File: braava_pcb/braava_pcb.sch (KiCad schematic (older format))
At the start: 49 parts, among them J1 Conn_01x18, J2 Conn_01x18

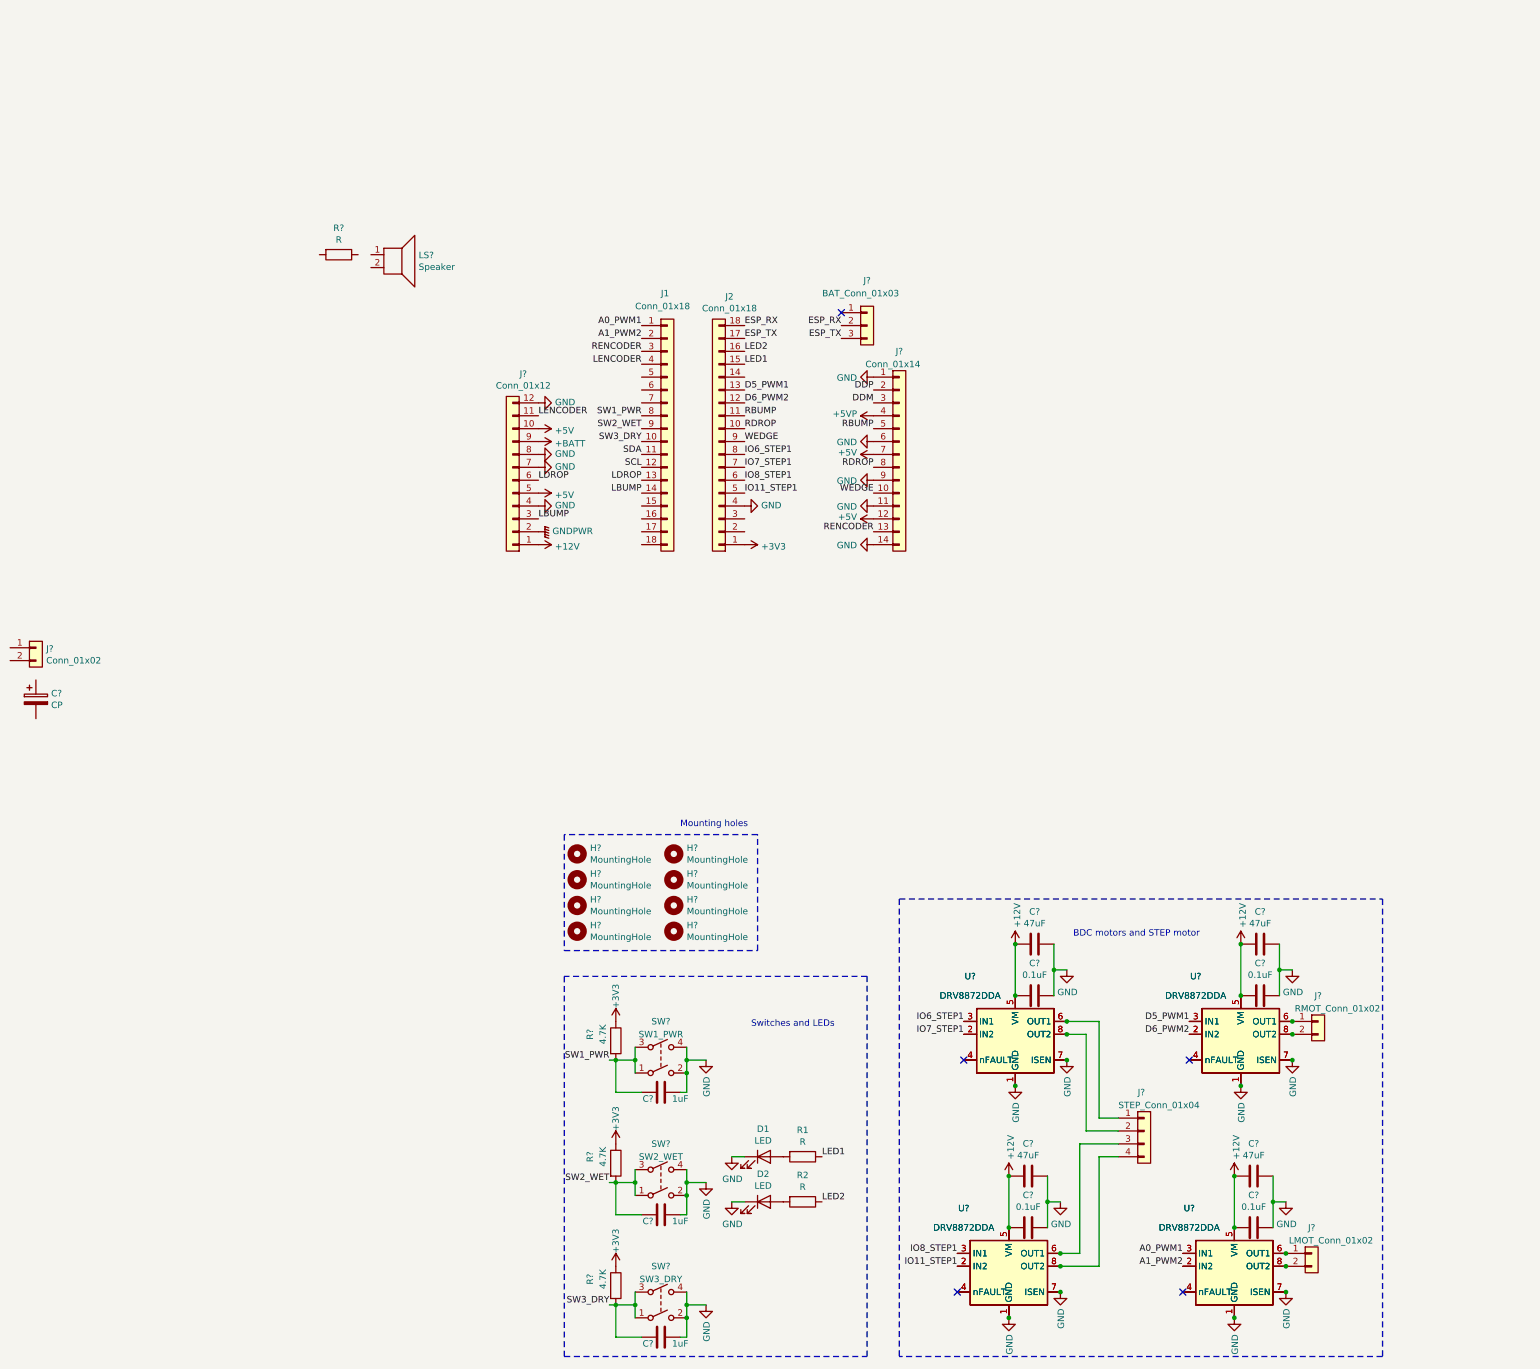
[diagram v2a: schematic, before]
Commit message: Added touch switches library. Started component placement.
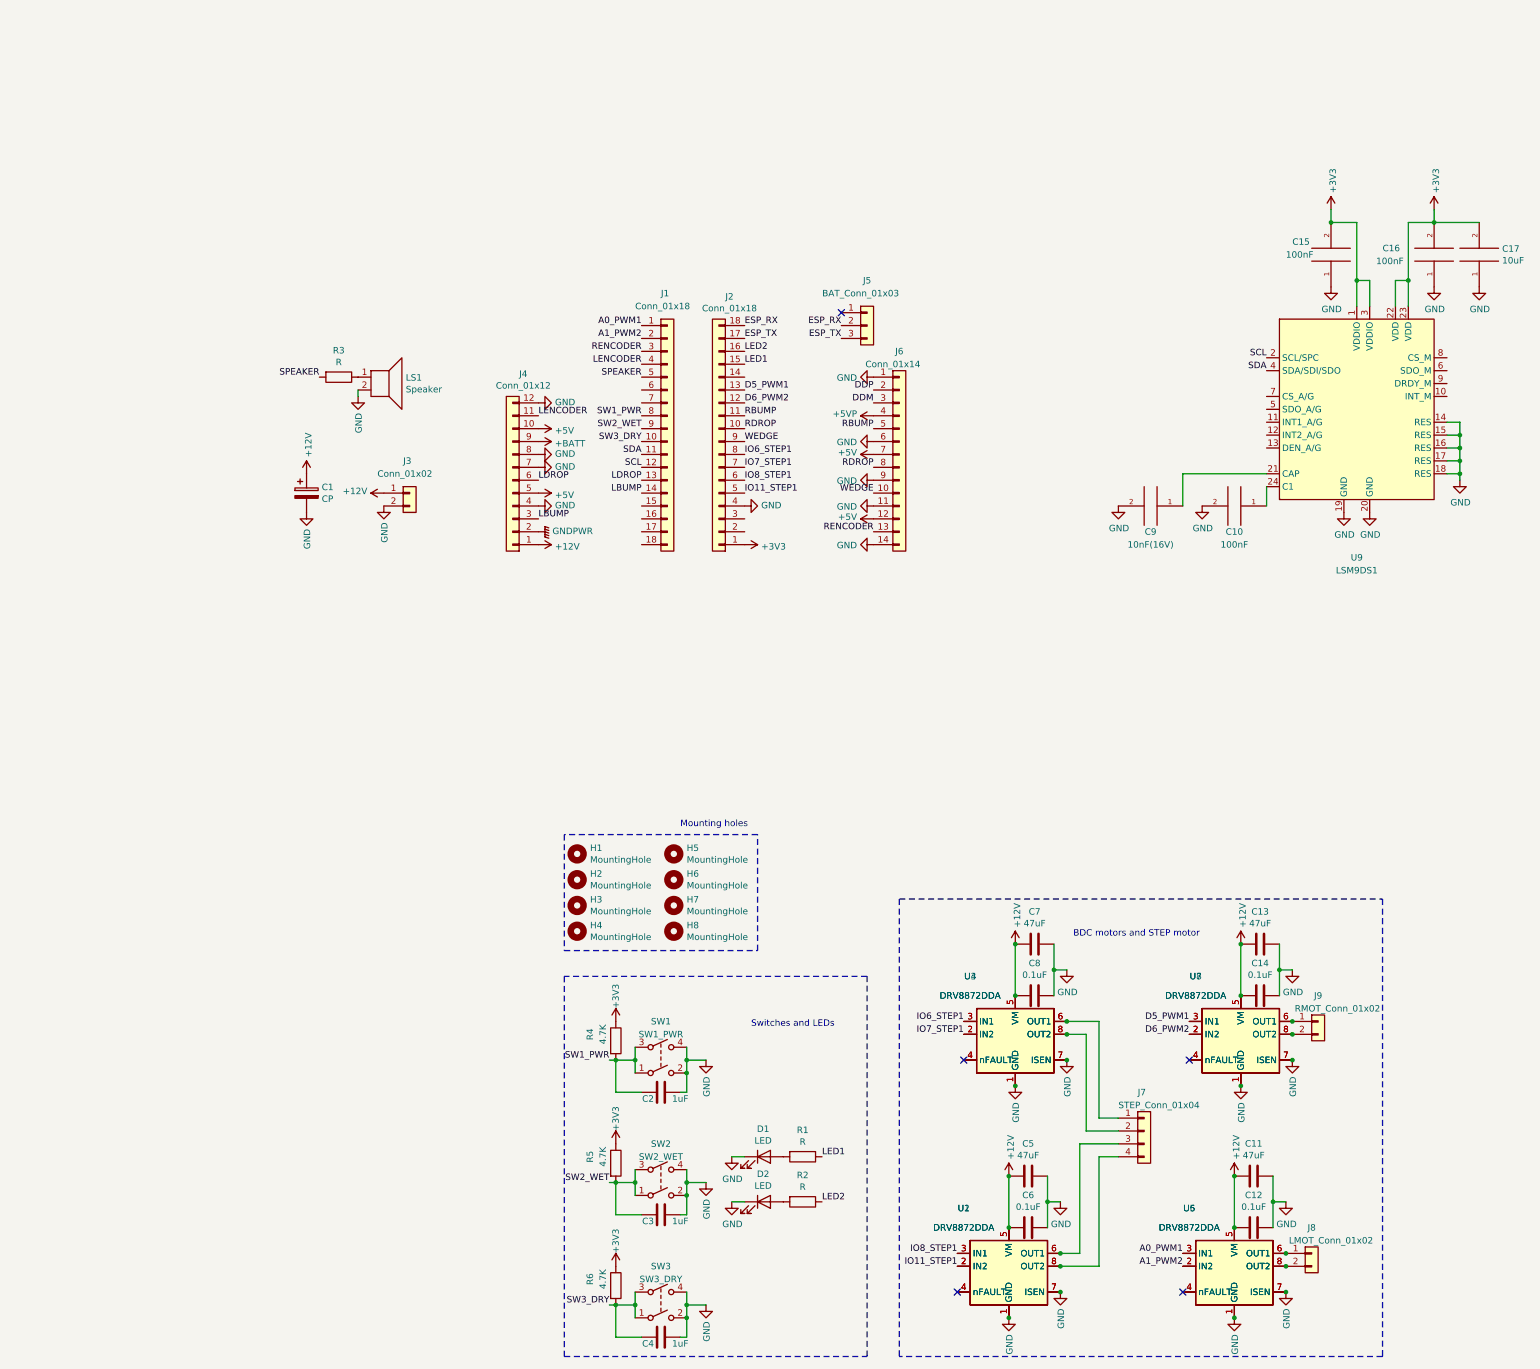
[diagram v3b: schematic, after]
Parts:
- added C10, C15, C16: 100nF, Capacitor_SMD:C_0603_1608Metric, symbol pspice:C
- added C17: 10uF, Capacitor_SMD:C_0603_1608Metric, symbol pspice:C
- added C9: 10nF(16V), Capacitor_SMD:C_0603_1608Metric, symbol pspice:C
- added U9: LSM9DS1, Package_LGA:LGA-24L_3x3.5mm_P0.43mm, symbol Sensor_Motion:LSM9DS1
- C1: renamed from C?; footprint (none) -> Capacitor_THT:CP_Radial_D8.0mm_P3.50mm
- C11, C12, C13, C14, C2, C3, C4, C5, C6, C7, C8: renamed from C?; footprint (none) -> Capacitor_SMD:C_0603_1608Metric
- H1, H2, H3, H4, H5, H6: renamed from H?; footprint (none) -> MountingHole:MountingHole_2.5mm
- H7, H8: renamed from H?; footprint (none) -> MountingHole:MountingHole_2.1mm
- J1, J2: footprint Connector_PinHeader_1.27mm:PinHeader_1x18_P1.27mm_Vertical -> Connector_PinHeader_2.54mm:PinHeader_1x18_P2.54mm_Vertical
- J3, J8, J9: renamed from J?; footprint (none) -> Connector_JST:JST_PH_B2B-PH-K_1x02_P2.00mm_Vertical
- J4: renamed from J?; footprint (none) -> Connector_JST:JST_PH_B12B-PH-K_1x12_P2.00mm_Vertical
- J5: renamed from J?; footprint (none) -> Connector_JST:JST_PH_B3B-PH-K_1x03_P2.00mm_Vertical
- J6: renamed from J?; footprint (none) -> Connector_JST:JST_PH_B14B-PH-K_1x14_P2.00mm_Vertical
- J7: renamed from J?; footprint (none) -> Connector_PinHeader_2.54mm:PinHeader_1x04_P2.54mm_Vertical
- LS1: renamed from LS?; footprint (none) -> Buzzer_Beeper:Buzzer_15x7.5RM7.6
- gave numbers to parts that had none: 15
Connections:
- net +12V: now also C1.1, J3.1 (Pin_1)
- net +3V3: now also C15.2, C16.2, C17.2, U9.1 (VDDIO), U9.22 (VDD), U9.23 (VDD), U9.3 (VDDIO)
- net GND: now also C1.2, J3.2 (Pin_2), LS1.2, C10.2, C15.1, C16.1, C17.1, C9.2, U9.14 (RES), U9.15 (RES), U9.16 (RES), U9.17 (RES), U9.18 (RES), U9.19 (GND), U9.20 (GND)
- net SCL: now also U9.2 (SCL/SPC)
- net SDA: now also U9.4 (SDA/SDI/SDO)
- net SPEAKER: now reaches J1.5 (Pin_5)
- net SPEAKER: now also R3.2
- net at LS1.1: now also R3.1
- new net: C9.1, U9.21 (CAP)
- new net: C10.1, U9.24 (C1)
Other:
- moved on the sheet: C1, J3, LS1, R3
